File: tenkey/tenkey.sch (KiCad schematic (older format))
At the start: 35 parts, among them SW0:0 NUM_0, SW0:2 DOT, SW1:0 NUM_1, SW1:1 NUM_2, SW1:2 NUM_3, SW1:4 ENTER, SW2:0 NUM_4, SW2:1 NUM_5, SW2:2 NUM_6, SW3:0 NUM_7, SW3:1 NUM_8, SW3:2 NUM_9, SW3:4 PLUS, SW4:0 NUM_LCK, SW4:1 DIVIDE, SW4:2 MULTIPLY, SW4:4 MINUS

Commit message: hopefully have a working schematic
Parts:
- removed IC?: ATMEGA328-P, DIL28, symbol ATMEGA328-P
- added D18, D19: LED, symbol LED
- added R1, R2: 220, symbol R
- added U1: TEENSY2.0, symbol TEENSY2.0
- gave numbers to parts that had none: 17
- renumbered SW1:4 to SW1:3, SW3:4 to SW3:3, SW4:4 to SW4:3
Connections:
- net labels added: GND, LED_A, LED_B, VCC
- no-connect marks 0 -> 16
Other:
- moved on the sheet: D0:0, D0:2, D1:0, D1:1, D1:2, D1:3, D2:0, D2:1, D2:2, D3:0, D3:1, D3:2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

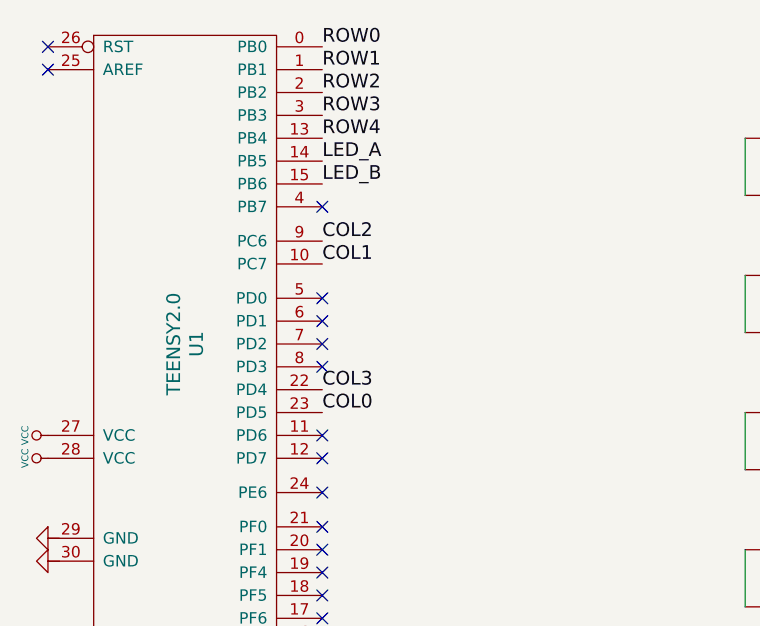
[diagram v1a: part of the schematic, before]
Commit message: Fixed pinout on the Teensy2.0 module and updated the tenkey schematic/board
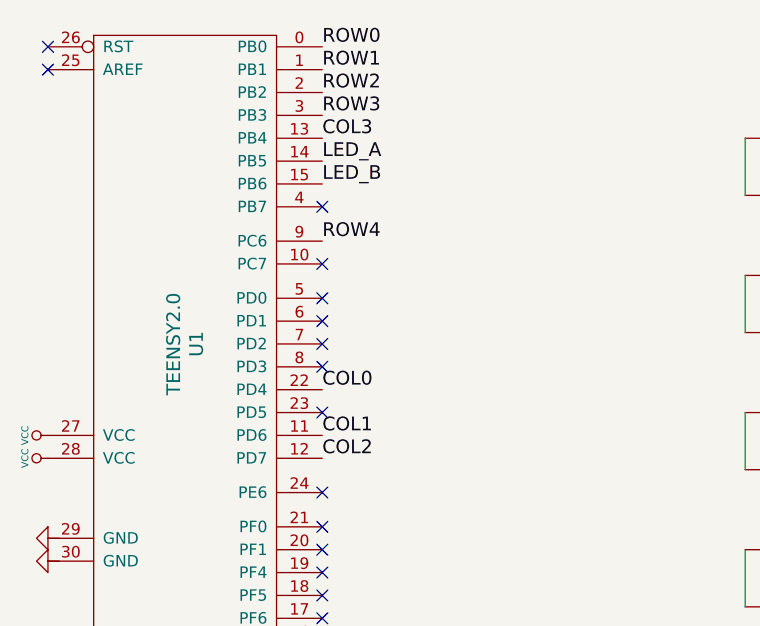
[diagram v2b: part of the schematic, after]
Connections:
- net COL0: now also U1.22 (PD4); no longer U1.23 (PD5)
- net COL1: now also U1.11 (PD6); no longer U1.10 (PC7)
- net COL2: now also U1.12 (PD7); no longer U1.9 (PC6)
- net COL3: now also U1.13 (PB4); no longer U1.22 (PD4)
- net ROW4: now also U1.9 (PC6); no longer U1.13 (PB4)
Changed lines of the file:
@@
 Text Label 3650 2350 0    60   ~ 0
 ROW3
+Text Label 3650 2900 0    60   ~ 0
+ROW4
+Text Label 3650 3550 0    60   ~ 0
+COL0
+Text Label 3650 3750 0    60   ~ 0
+COL1
+Text Label 3650 3850 0    60   ~ 0
+COL2
 Text Label 3650 2450 0    60   ~ 0
-ROW4
-Text Label 3650 3650 0    60   ~ 0
-COL0
-Text Label 3650 3000 0    60   ~ 0
-COL1
-Text Label 3650 2900 0    60   ~ 0
-COL2
-Text Label 3650 3550 0    60   ~ 0
 COL3
 NoConn ~ 2450 2050
@@
 NoConn ~ 3650 3350
 NoConn ~ 3650 3450
-NoConn ~ 3650 3750
-NoConn ~ 3650 3850
+NoConn ~ 3650 3650
+NoConn ~ 3650 3000
 NoConn ~ 3650 4000
 NoConn ~ 3650 4150

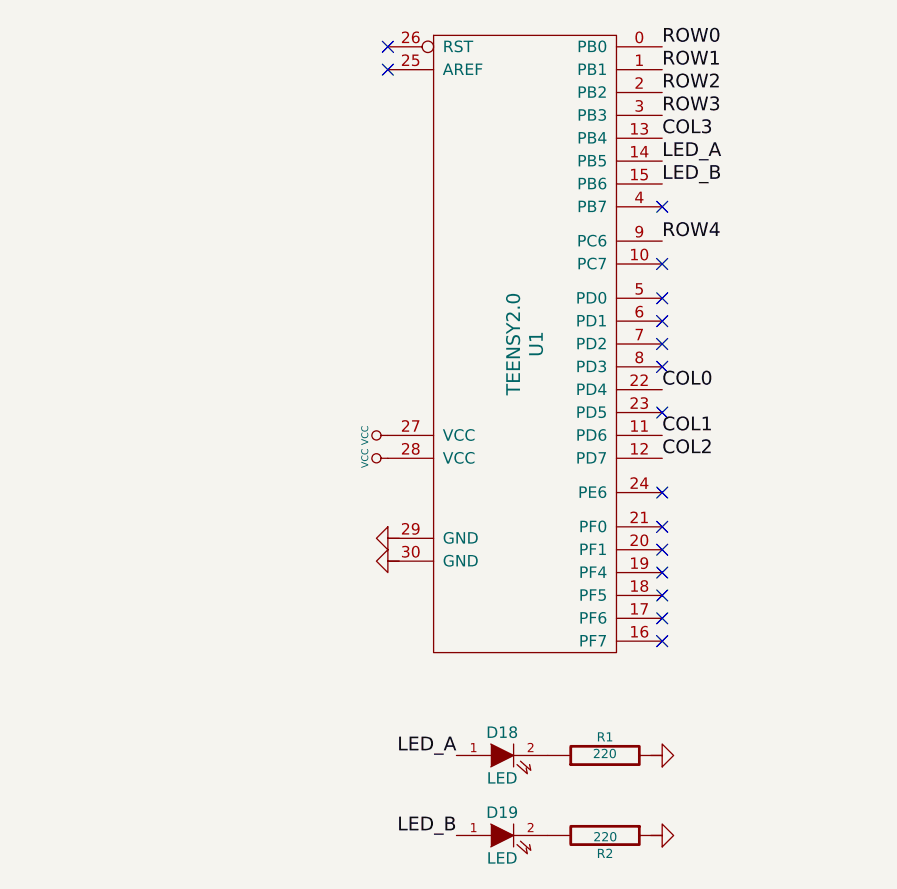
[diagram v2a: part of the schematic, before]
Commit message: tenkey finished pcb routing and adjusting pinout
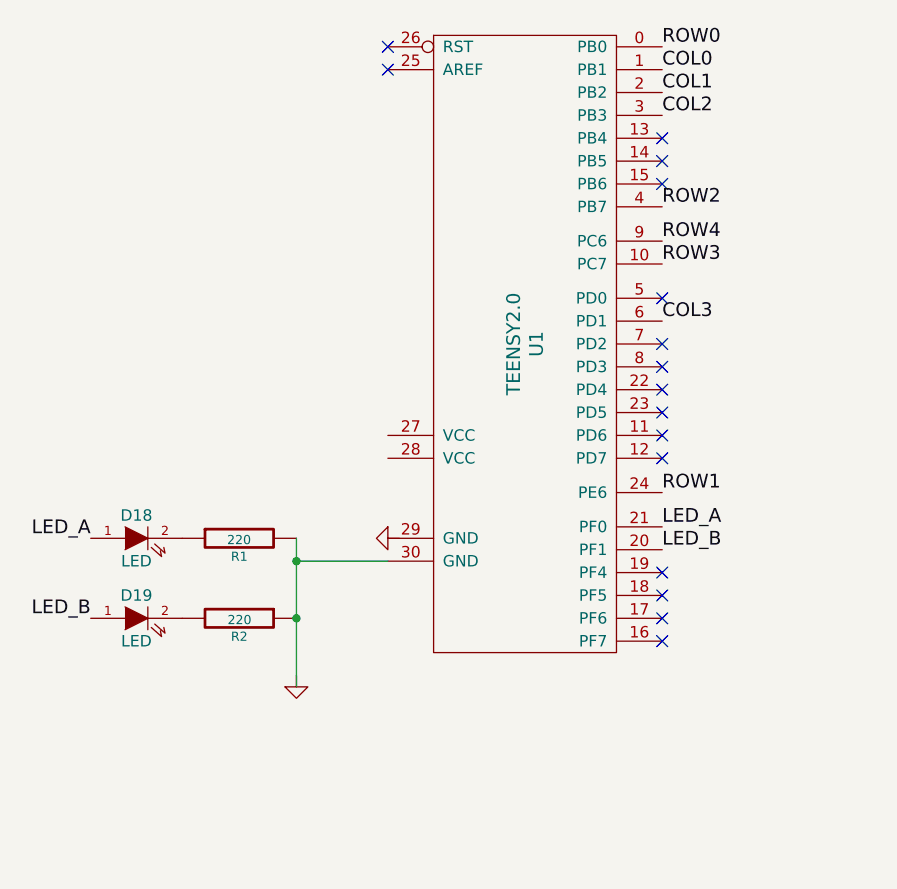
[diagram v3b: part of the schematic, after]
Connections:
- net COL0: now also U1.1 (PB1); no longer U1.22 (PD4)
- net COL1: now also U1.2 (PB2); no longer U1.11 (PD6)
- net COL2: now also U1.3 (PB3); no longer U1.12 (PD7)
- net COL3: now also U1.6 (PD1); no longer U1.13 (PB4)
- net LED_A: now also U1.21 (PF0); no longer U1.14 (PB5)
- net LED_B: now also U1.20 (PF1); no longer U1.15 (PB6)
- net ROW1: now also U1.24 (PE6); no longer U1.1 (PB1)
- net ROW2: now also U1.4 (PB7); no longer U1.2 (PB2)
- net ROW3: now also U1.10 (PC7); no longer U1.3 (PB3)
- net at U1.30 (GND): now also R1.2, R2.1
- net VCC: no longer names the net of U1.27 (VCC)
- net VCC: no longer U1.28 (VCC)
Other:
- moved on the sheet: D18, D19, R1, R2
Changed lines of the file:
@@
 $EndComp
 $Comp
-L VCC #PWR01
-U 1 1 56FF26B7
-P 2450 3750
-F 0 "#PWR01" H 2450 3850 30  0001 C CNN
-F 1 "VCC" H 2450 3850 30  0000 C CNN
-F 2 "" H 2450 3750 60  0000 C CNN
-F 3 "" H 2450 3750 60  0000 C CNN
-	1    2450 3750
-	0    -1   -1   0
-$EndComp
-$Comp
-L GND #PWR02
+L GND #PWR01
 U 1 1 56FF26E9
 P 2450 4200
-F 0 "#PWR02" H 2450 4200 30  0001 C CNN
+F 0 "#PWR01" H 2450 4200 30  0001 C CNN
 F 1 "GND" H 2450 4130 30  0001 C CNN
 F 2 "" H 2450 4200 60  0000 C CNN
@@
 L LED D18
 U 1 1 56FF27A7
-P 2950 5150
-F 0 "D18" H 2950 5250 50  0000 C CNN
-F 1 "LED" H 2950 5050 50  0000 C CNN
-F 2 "" H 2950 5150 60  0000 C CNN
-F 3 "" H 2950 5150 60  0000 C CNN
-	1    2950 5150
+P 1350 4200
+F 0 "D18" H 1350 4300 50  0000 C CNN
+F 1 "LED" H 1350 4100 50  0000 C CNN
+F 2 "" H 1350 4200 60  0000 C CNN
+F 3 "" H 1350 4200 60  0000 C CNN
+	1    1350 4200
 	1    0    0    -1
 $EndComp
@@
 L LED D19
 U 1 1 56FF27BB
-P 2950 5500
-F 0 "D19" H 2950 5600 50  0000 C CNN
-F 1 "LED" H 2950 5400 50  0000 C CNN
-F 2 "" H 2950 5500 60  0000 C CNN
-F 3 "" H 2950 5500 60  0000 C CNN
-	1    2950 5500
+P 1350 4550
+F 0 "D19" H 1350 4650 50  0000 C CNN
+F 1 "LED" H 1350 4450 50  0000 C CNN
+F 2 "" H 1350 4550 60  0000 C CNN
+F 3 "" H 1350 4550 60  0000 C CNN
+	1    1350 4550
 	1    0    0    -1
 $EndComp
@@
 L R R1
 U 1 1 56FF27CF
-P 3400 5150
-F 0 "R1" V 3480 5150 40  0000 C CNN
-F 1 "220" V 3407 5151 40  0000 C CNN
-F 2 "" V 3330 5150 30  0000 C CNN
-F 3 "" H 3400 5150 30  0000 C CNN
-	1    3400 5150
-	0    -1   -1   0
+P 1800 4200
+F 0 "R1" V 1880 4200 40  0000 C CNN
+F 1 "220" V 1807 4201 40  0000 C CNN
+F 2 "" V 1730 4200 30  0000 C CNN
+F 3 "" H 1800 4200 30  0000 C CNN
+	1    1800 4200
+	0    -1   1    0
 $EndComp
 $Comp
 L R R2
 U 1 1 56FF27E3
-P 3400 5500
-F 0 "R2" V 3480 5500 40  0000 C CNN
-F 1 "220" V 3407 5501 40  0000 C CNN
-F 2 "" V 3330 5500 30  0000 C CNN
-F 3 "" H 3400 5500 30  0000 C CNN
-	1    3400 5500
+P 1800 4550
+F 0 "R2" V 1880 4550 40  0000 C CNN
+F 1 "220" V 1807 4551 40  0000 C CNN
+F 2 "" V 1730 4550 30  0000 C CNN
+F 3 "" H 1800 4550 30  0000 C CNN
+	1    1800 4550
 	0    1    1    0
 $EndComp
-$Comp
-L GND #PWR03
-U 1 1 56FF27F7
-P 3650 5500
-F 0 "#PWR03" H 3650 5500 30  0001 C CNN
-F 1 "GND" H 3650 5430 30  0001 C CNN
-F 2 "" H 3650 5500 60  0000 C CNN
-F 3 "" H 3650 5500 60  0000 C CNN
-	1    3650 5500
-	0    -1   -1   0
-$EndComp
-$Comp
-L GND #PWR04
-U 1 1 56FF280B
-P 3650 5150
-F 0 "#PWR04" H 3650 5150 30  0001 C CNN
-F 1 "GND" H 3650 5080 30  0001 C CNN
-F 2 "" H 3650 5150 60  0000 C CNN
-F 3 "" H 3650 5150 60  0000 C CNN
-	1    3650 5150
-	0    -1   -1   0
-$EndComp
-Text Label 2750 5150 2    60   ~ 0
+Text Label 1150 4200 2    60   ~ 0
 LED_A
-Text Label 2750 5500 2    60   ~ 0
+Text Label 1150 4550 2    60   ~ 0
 LED_B
-Text Label 3650 2550 0    60   ~ 0
+Text Label 3650 4150 0    60   ~ 0
 LED_A
-Text Label 3650 2650 0    60   ~ 0
+Text Label 3650 4250 0    60   ~ 0
 LED_B
 Text Label 3650 2050 0    60   ~ 0
 ROW0
-Text Label 3650 2150 0    60   ~ 0
+Text Label 3650 4000 0    60   ~ 0
 ROW1
-Text Label 3650 2250 0    60   ~ 0
+Text Label 3650 2750 0    60   ~ 0
 ROW2
-Text Label 3650 2350 0    60   ~ 0
+Text Label 3650 3000 0    60   ~ 0
 ROW3
 Text Label 3650 2900 0    60   ~ 0
 ROW4
-Text Label 3650 3550 0    60   ~ 0
+Text Label 3650 2150 0    60   ~ 0
 COL0
-Text Label 3650 3750 0    60   ~ 0
+Text Label 3650 2250 0    60   ~ 0
 COL1
-Text Label 3650 3850 0    60   ~ 0
+Text Label 3650 2350 0    60   ~ 0
 COL2
-Text Label 3650 2450 0    60   ~ 0
+Text Label 3650 3250 0    60   ~ 0
 COL3
 NoConn ~ 2450 2050
 NoConn ~ 2450 2150
-NoConn ~ 3650 2750
+NoConn ~ 3650 3850
 NoConn ~ 3650 3150
-NoConn ~ 3650 3250
+NoConn ~ 3650 3550
 NoConn ~ 3650 3350
 NoConn ~ 3650 3450
 NoConn ~ 3650 3650
-NoConn ~ 3650 3000
-NoConn ~ 3650 4000
-NoConn ~ 3650 4150
-NoConn ~ 3650 4250
+NoConn ~ 3650 3750
+NoConn ~ 3650 2450
+NoConn ~ 3650 2550
+NoConn ~ 3650 2650
 NoConn ~ 3650 4350
 NoConn ~ 3650 4450
 NoConn ~ 3650 4550
 NoConn ~ 3650 4650
-$Comp
-L GND #PWR05
-U 1 1 56FF26FD
-P 2450 4300
-F 0 "#PWR05" H 2450 4300 30  0001 C CNN
-F 1 "GND" H 2450 4230 30  0001 C CNN
-F 2 "" H 2450 4300 60  0000 C CNN
-F 3 "" H 2450 4300 60  0000 C CNN
-	1    2450 4300
-	0    1    1    0
-$EndComp
 Wire Wire Line
 	5500 3050 5500 3300
@@
 Wire Wire Line
 	8650 4250 8650 2200
-$Comp
-L VCC #PWR06
-U 1 1 56FF26CB
-P 2450 3850
-F 0 "#PWR06" H 2450 3950 30  0001 C CNN
-F 1 "VCC" H 2450 3950 30  0000 C CNN
-F 2 "" H 2450 3850 60  0000 C CNN
-F 3 "" H 2450 3850 60  0000 C CNN
-	1    2450 3850
-	0    -1   -1   0
-$EndComp
+Wire Wire Line
+	2050 4200 2050 4850
+Connection ~ 2050 4550
+$Comp
+L GND #PWR02
+U 1 1 57055F56
+P 2050 4850
+F 0 "#PWR02" H 2050 4850 30  0001 C CNN
+F 1 "GND" H 2050 4780 30  0001 C CNN
+F 2 "" H 2050 4850 60  0000 C CNN
+F 3 "" H 2050 4850 60  0000 C CNN
+	1    2050 4850
+	1    0    0    -1
+$EndComp
+Wire Wire Line
+	2450 4300 2050 4300
+Connection ~ 2050 4300
 $EndSCHEMATC

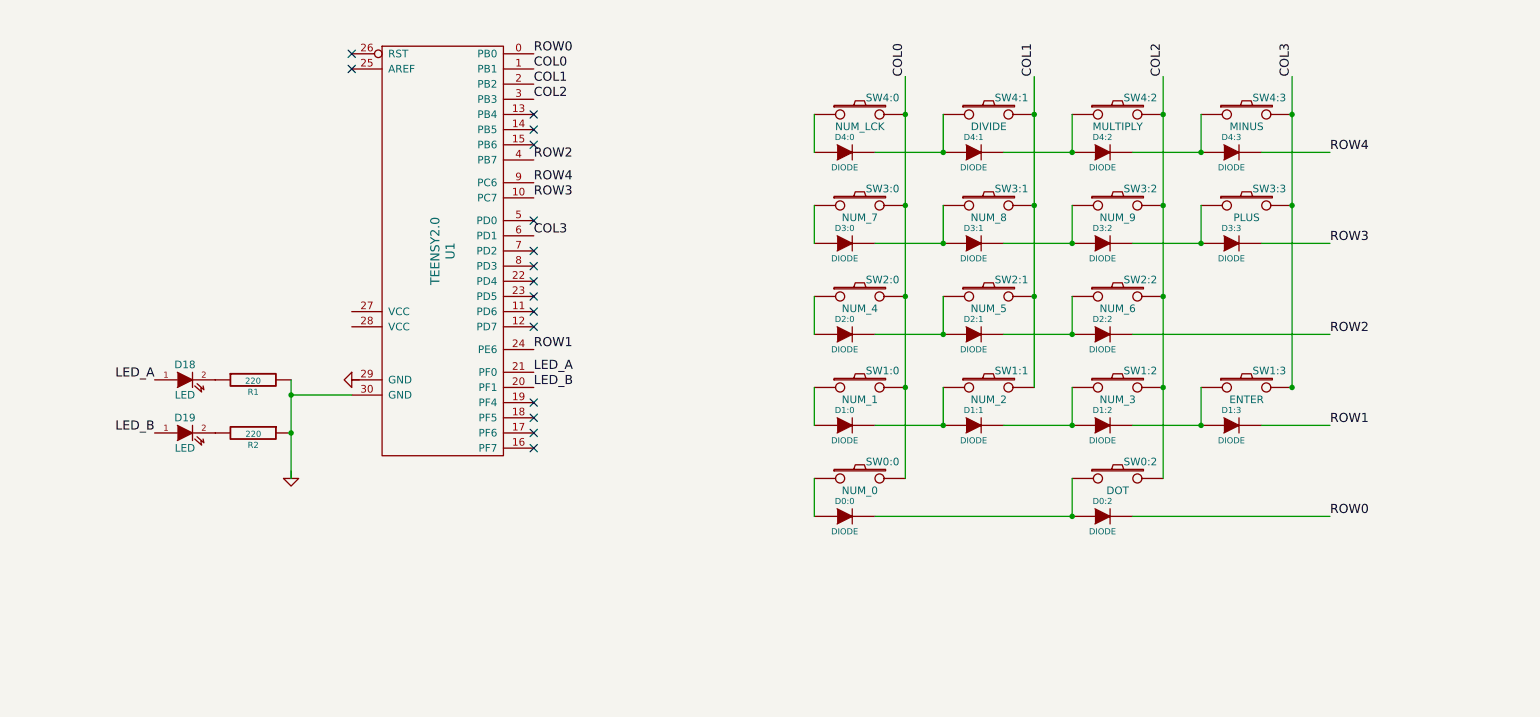
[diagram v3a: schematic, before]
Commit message: starting the embedding of a ATMega32U4 on the tenkey instead of a teensy
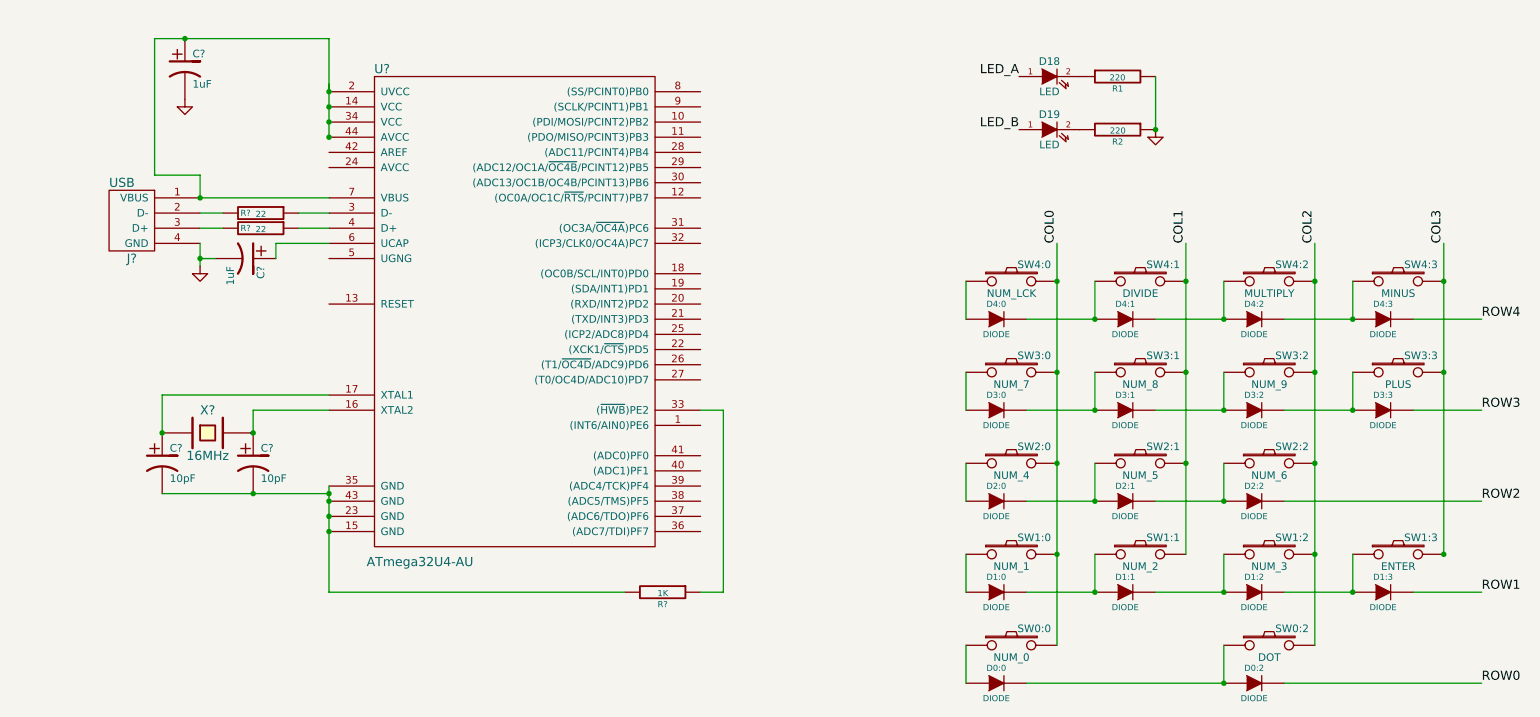
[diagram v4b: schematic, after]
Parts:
- removed U1: TEENSY2.0, symbol TEENSY2.0
- added C? (x2): 1uF, symbol CP1
- added C? (x2): 10pF, symbol CP1
- added J?: USB, symbol USB
- added R? (x2): 22, symbol R
- added R?: 1K, symbol R
- added U?: ATmega32U4-AU, symbol ATmega32U4-AU
- added X?: 16MHz, symbol CRYSTAL
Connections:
- net GND: now also R1.2, R2.1, C?.2, C?.2, J?.4 (GND)
- new net: C?.1, J?.1 (VBUS), U?.14 (VCC), U?.2 (UVCC), U?.34 (VCC), U?.44 (AVCC), U?.7 (VBUS)
- new net: C?.2, C?.2, R?.2, U?.15 (GND), U?.23 (GND), U?.35 (GND), U?.43 (GND)
- new net: C?.1, U?.16 (XTAL2), X?.2
- new net: C?.1, U?.17 (XTAL1), X?.1
- new net: R?.1, U?.3 (D-)
- new net: R?.1, U?.33 ((~HWB~)PE2)
- new net: R?.1, U?.4 (D+)
- new net: C?.1, U?.6 (UCAP)
- new net: J?.2 (D-), R?.2
- new net: J?.3 (D+), R?.2
- no-connect marks 16 -> 0
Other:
- moved on the sheet: D0:0, D0:2, D18, D19, D1:0, D1:1, D1:2, D1:3, D2:0, D2:1, D2:2, D3:0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

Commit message: teensie is gone, were building this with the straight ATMega32u4
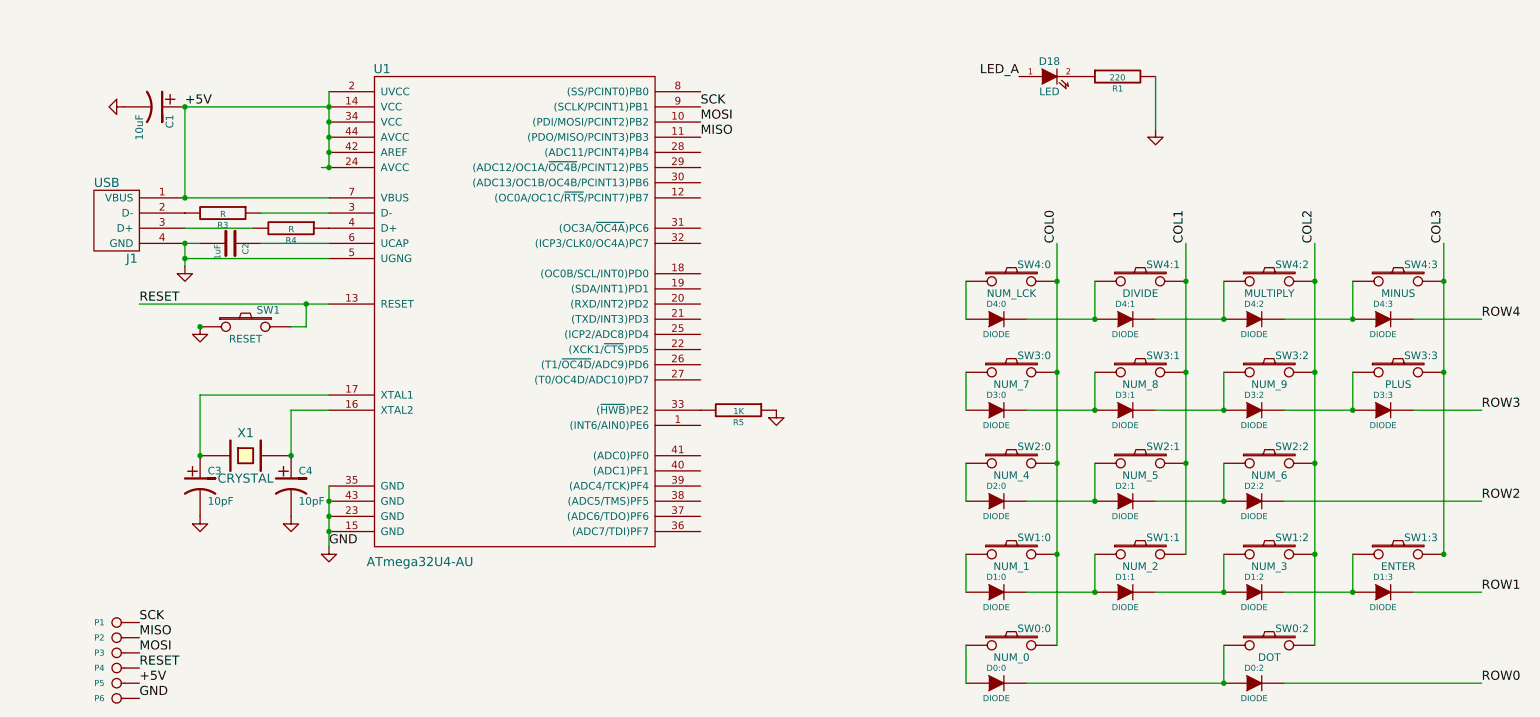
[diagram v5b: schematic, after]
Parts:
- removed C? (x2): 1uF, symbol CP1
- removed C? (x2): 10pF, symbol CP1
- removed D19: LED, symbol LED
- removed J?: USB, symbol USB
- removed R2: 220, symbol R
- removed R? (x2): 22, symbol R
- removed R?: 1K, symbol R
- removed X?: 16MHz, symbol CRYSTAL
- added C1: 10uF, symbol CP1
- added C2: 1uF, symbol C
- added C3, C4: 10pF, symbol CP1
- added J1: USB, symbol USB
- added P1: SCK, symbol CONN_1
- added P2: MISO, symbol CONN_1
- added P3: MOSI, symbol CONN_1
- added P4: RESET, symbol CONN_1
- added P5: 5V, symbol CONN_1
- added P6: GND, symbol CONN_1
- added R3, R4: R, symbol R
- added R5: 1K, symbol R
- added SW1: RESET, symbol SW_PUSH
- added X1: CRYSTAL, symbol CRYSTAL
- gave numbers to parts that had none: 1
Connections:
- net GND: now also U1.15 (GND), U1.23 (GND), U1.35 (GND), U1.43 (GND), U1.5 (UGNG), C1.2, C2.2, C3.2, C4.2, J1.4 (GND), P6.1, R5.1, SW1.1
- net MOSI: now reaches U1.10 ((PDI/MOSI/PCINT2)PB2)
- net MOSI: now also P3.1
- net MISO: now reaches U1.11 ((PDO/MISO/PCINT3)PB3)
- net MISO: now also P2.1
- net RESET: now reaches U1.13 (RESET)
- net RESET: now also P4.1, SW1.2
- net +5V: now reaches U1.14 (VCC), U1.2 (UVCC), U1.34 (VCC), U1.44 (AVCC), U1.7 (VBUS)
- net +5V: now also U1.24 (AVCC), U1.42 (AREF), C1.1, J1.1 (VBUS), P5.1
- net at U1.16 (XTAL2): now also C4.1, X1.2
- net at U1.17 (XTAL1): now also C3.1, X1.1
- net at U1.3 (D-): now also R3.1
- net at U1.33 ((~HWB~)PE2): now also R5.2
- net at U1.4 (D+): now also R4.1
- net at U1.6 (UCAP): now also C2.1
- net SCK: now reaches U1.9 ((SCLK/PCINT1)PB1)
- net SCK: now also P1.1
- new net: J1.2 (D-), R3.2
- new net: J1.3 (D+), R4.2
